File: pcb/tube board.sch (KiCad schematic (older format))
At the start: 39 parts, among them J6 Conn_02x06_Counter_Clockwise, J7 Conn_02x12_Counter_Clockwise, Q10 ZVP1320F, Q11 BSS127S, Q12 ZVN3320F, Q13 BSS127S, Q14 BSS127S, Q15 ZVP1320F, Q16 BSS127S, Q17 BSS127S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

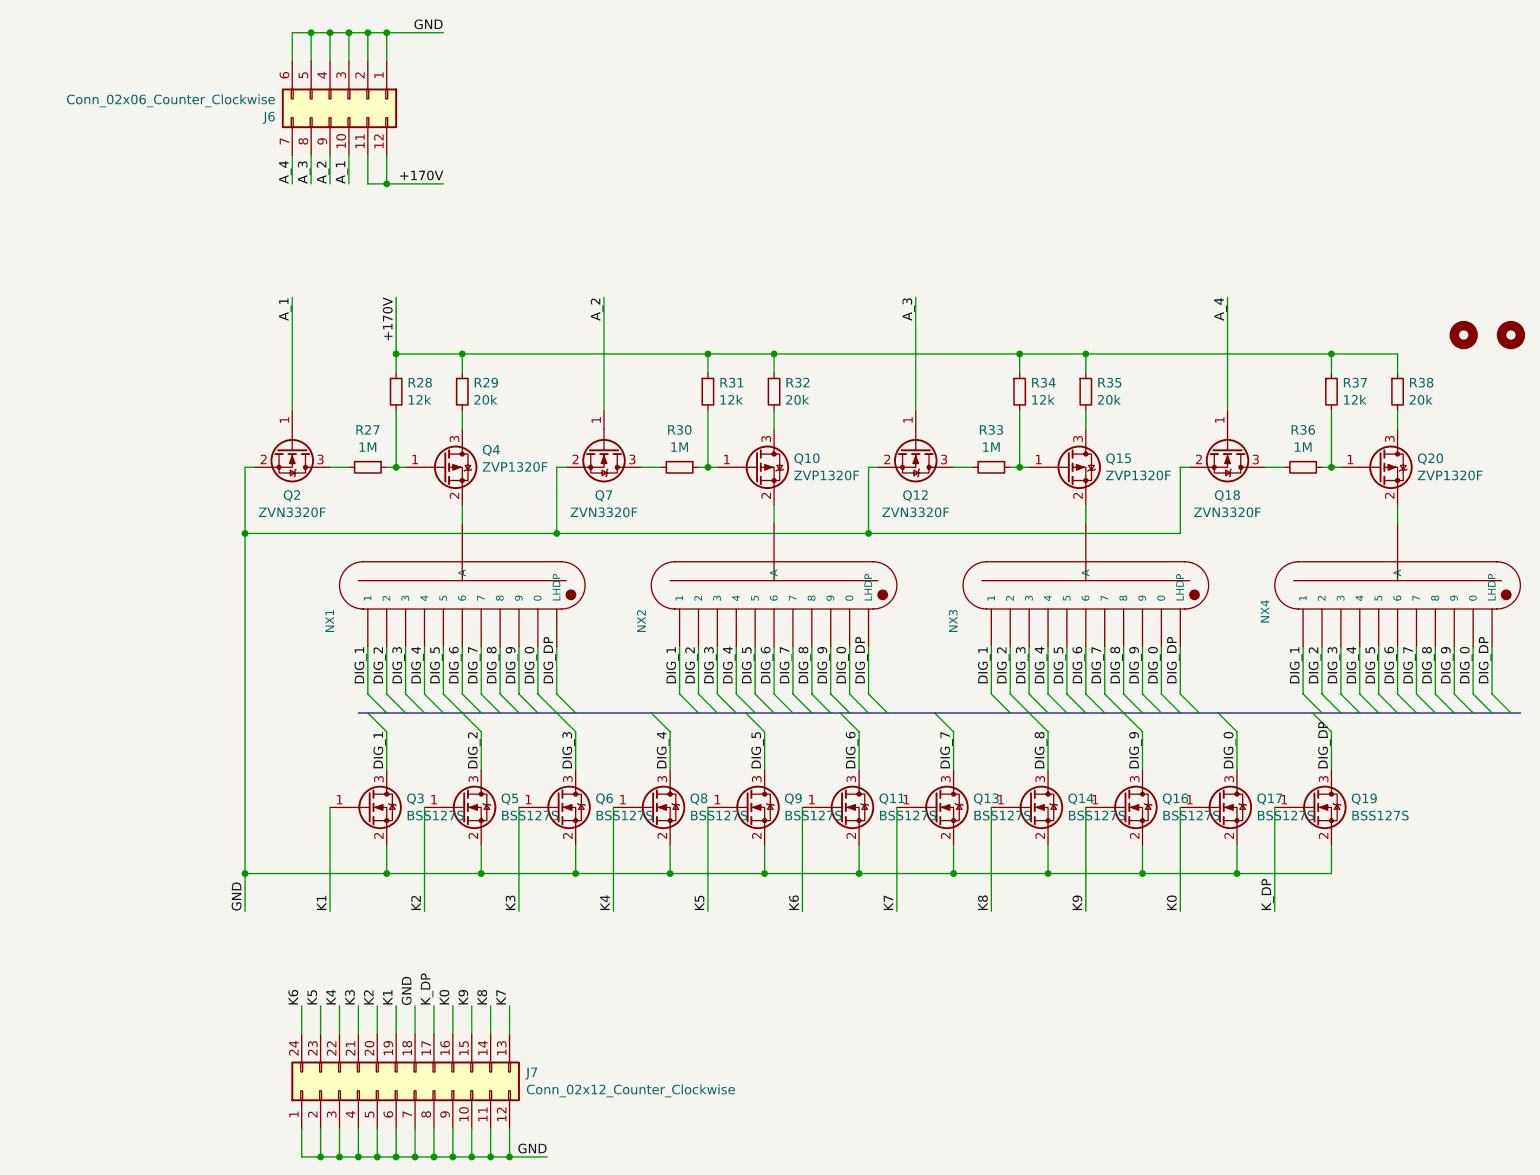
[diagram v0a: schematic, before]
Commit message: Update PCB and schematic files with mostly small tweaks. Added DRC rules added to .pro, and changes on layout and footprints to reflect that.
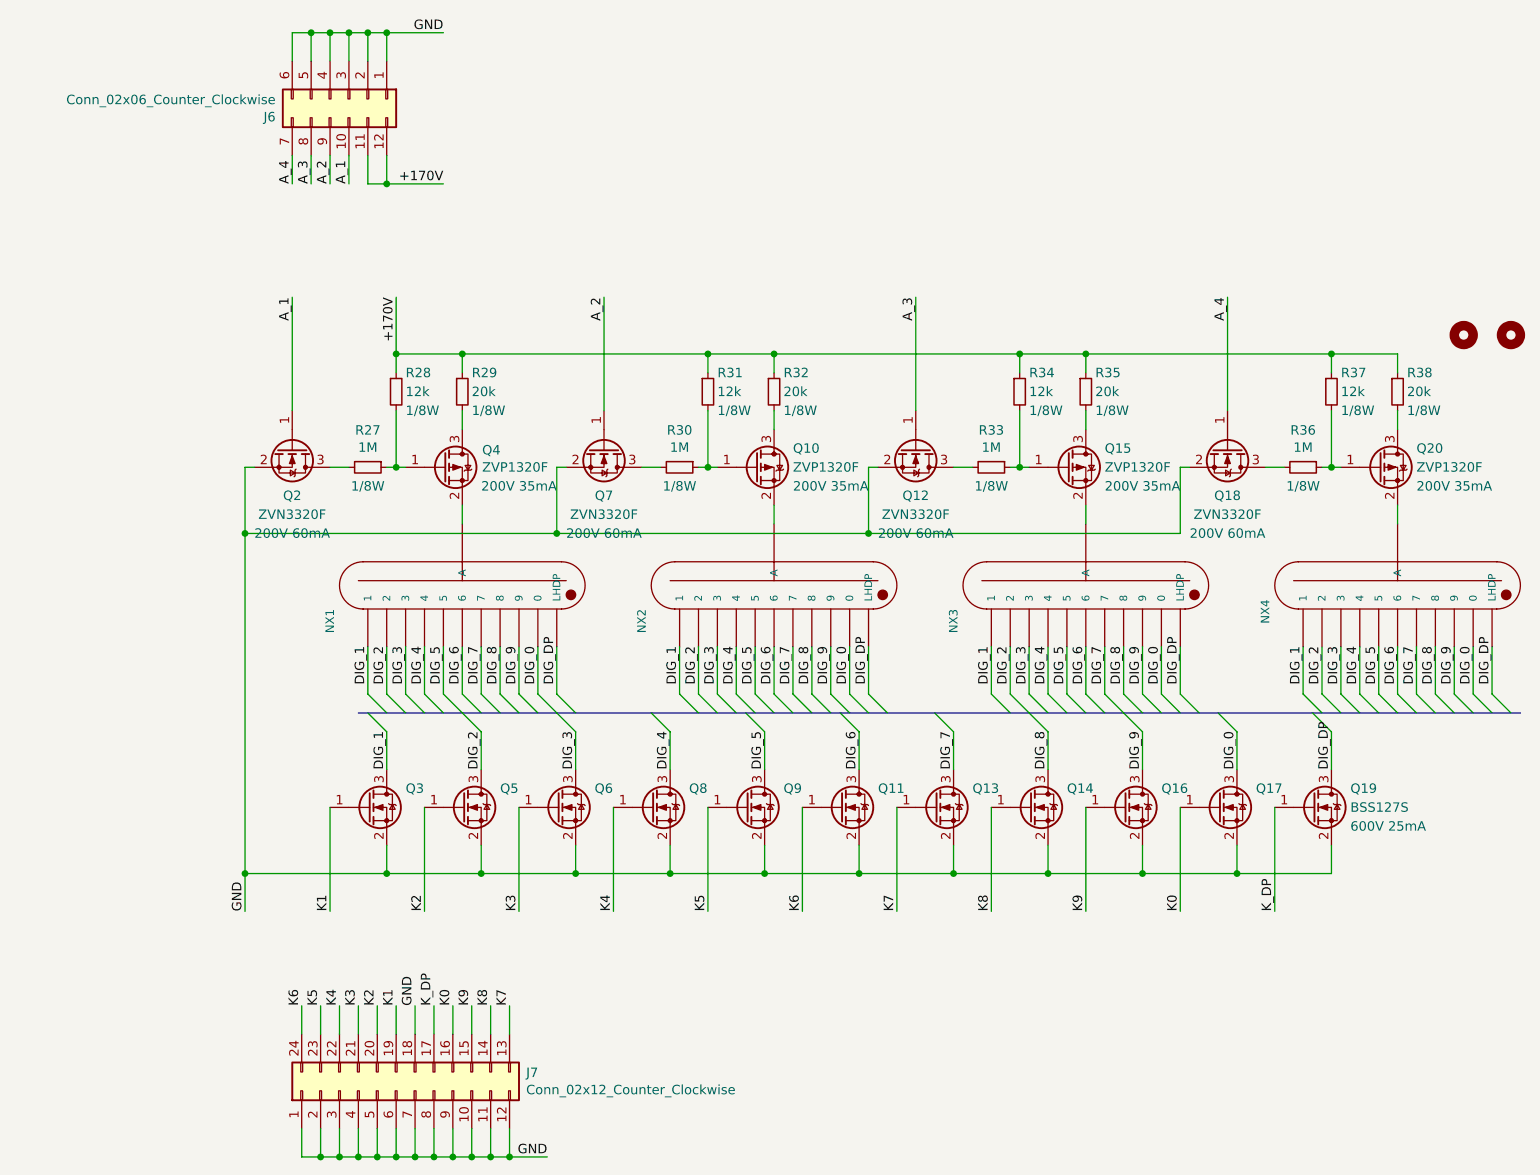
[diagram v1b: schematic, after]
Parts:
- H5, H6: Rating (none) -> N/A
- J6, J7: Digikey Page (none) -> N/A; Rating (none) -> N/A
- NX1, NX2, NX3, NX4: Rating (none) -> 170V
- Q10, Q15, Q20, Q4: Rating (none) -> 200V 35mA
- Q11, Q13, Q14, Q16, Q17, Q19, Q3, Q5, Q6, Q8, Q9: Rating (none) -> 600V 25mA
- Q12, Q18, Q2, Q7: Rating (none) -> 200V 60mA
- R27, R28, R29, R30, R31, R32, R33, R34, R35, R36, R37, R38: Rating (none) -> 1/8W

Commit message: Add alternate parts for BOM, adjust micro to be more compatible with new PIC24FJ series parts.
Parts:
- H5, H6, J6, J7, NX1, NX2, NX3, NX4, R27, R28, R29, R30, R31, R32, R33, R34, R35, R36, R37, R38: Alt Datasheet (none) -> -; Alt Digikey (none) -> -
- Q10, Q15, Q20, Q4: Alt Datasheet (none) -> https://ww1.microchip.com/downloads/en/DeviceDoc/TP5335-P-C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; Alt Digikey (none) -> https://www.digikey.com/en/products/detail/microchip-techno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
- Q11, Q12, Q13, Q14, Q16, Q17, Q18, Q19, Q2, Q3, Q5, Q6, Q7, Q8, Q9: Alt Datasheet (none) -> https://www.diodes.com/assets/Datasheets/BSS127.pdf; Alt Digikey (none) -> https://www.digikey.com/en/products/detail/diodes-incorpora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
